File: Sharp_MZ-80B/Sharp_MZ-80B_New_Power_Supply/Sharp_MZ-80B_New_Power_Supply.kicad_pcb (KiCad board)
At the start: 2 copper layers, 139 x 125 mm, 19 parts, among them J1 +12V (NS), J2 DC In, J3 To Tape Deck, J4 To Motherboard, U1 PSU5, U2 R-78CK5.0-0.5

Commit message: Revised PSU design
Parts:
- added D2: 1.5KE15A, Diode_THT:D_DO-201AE_P15.24mm_Horizontal, F.Cu at (107.6, 56.2)
- added F1: T4A, Fuse:Littelfuse_5x20mm, F.Cu at (93.0, 67.4)
- C1: value 4700µF -> 4700µF 25V; footprint Capacitor_THT:CP_Radial_D16.0mm_P7.50mm -> Capacitor_THT:CP_Axial_L40.0mm_D16.0mm_P48.00mm_Horizontal
- C2, C4, C6, C8: footprint Capacitor_THT:C_Disc_D3.8mm_W2.6mm_P2.50mm -> Capacitor_THT:C_Disc_D4.7mm_W2.5mm_P5.00mm
- J1: value +12V (NS) -> +12V (S)
- J2: footprint Clueless_Engineer:TJC1-2A -> Connector_JST:JST_VH_B2P-VH_1x02_P3.96mm_Vertical
- R1: value 2.2Ω -> 2.2Ω 2W
- moved C1 56.8 mm to (208.6, 56.2)
- moved D1 54.3 mm to (172.4, 56.2)
- moved R1 53.6 mm to (178.1, 56.2)
- moved C4 40.4 mm to (137.5, 56.2), turned to -90 degrees
- moved C3 39.6 mm to (123.5, 56.2), turned to -90 degrees
- moved J1 29.8 mm to (147.6, 56.2)
- moved C2 29.3 mm to (193.3, 64.4)
- moved J3 24.4 mm to (147.6, 71.4)
- moved C5 17.9 mm to (117.7, 105.7)
- moved C6 17.3 mm to (115.2, 113.3)
- moved U2 16.0 mm to (112.7, 95.5)
- moved J2 10.2 mm to (93.0, 94.4), turned to 90 degrees
- moved C7 4.49 mm to (169.2, 111.4)
- moved J4 4.44 mm to (151.9, 144.4)
- moved U1 3.24 mm to (140.5, 111.4)
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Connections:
- J1 pad 1: /+12V NS -> /+12V
- J2 pad 2: /+12V -> /+12V_{IN}
- J3 pad 3: /+12V -> /+12V NS
- J4 pad 2: /-5V -> /+5V
- J4 pad 3: /+5V -> /+12V
- J4 pad 4: /+12V -> /-5V
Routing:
- net /GND: track 608.0 -> 542.3 mm
- net /+12V: track 237.5 -> 276.5 mm
- net /-5V: track 76.8 -> 115.0 mm
- net /+12V NS: track 36.8 -> 57.5 mm
- net /+5V: track 132.2 -> 112.1 mm
- net /+12V_{IN}: track 0.00 -> 11.8 mm
- net Net-(D1-K): track 6.35 -> 5.72 mm
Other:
- board text added: "+5V GND +12V (NS)"
- board text added: "GND +5V +12V (S) -5V"
- board text removed: "+5V GND +12V"
- board text removed: "Connectors: TJC1 5V Regulator: PSU5 No Noise (ezsbc.com) -5V Regulator: R-78CK5.0-0.5 (Recom)"
- board text removed: "GND -5V +5V +12V"

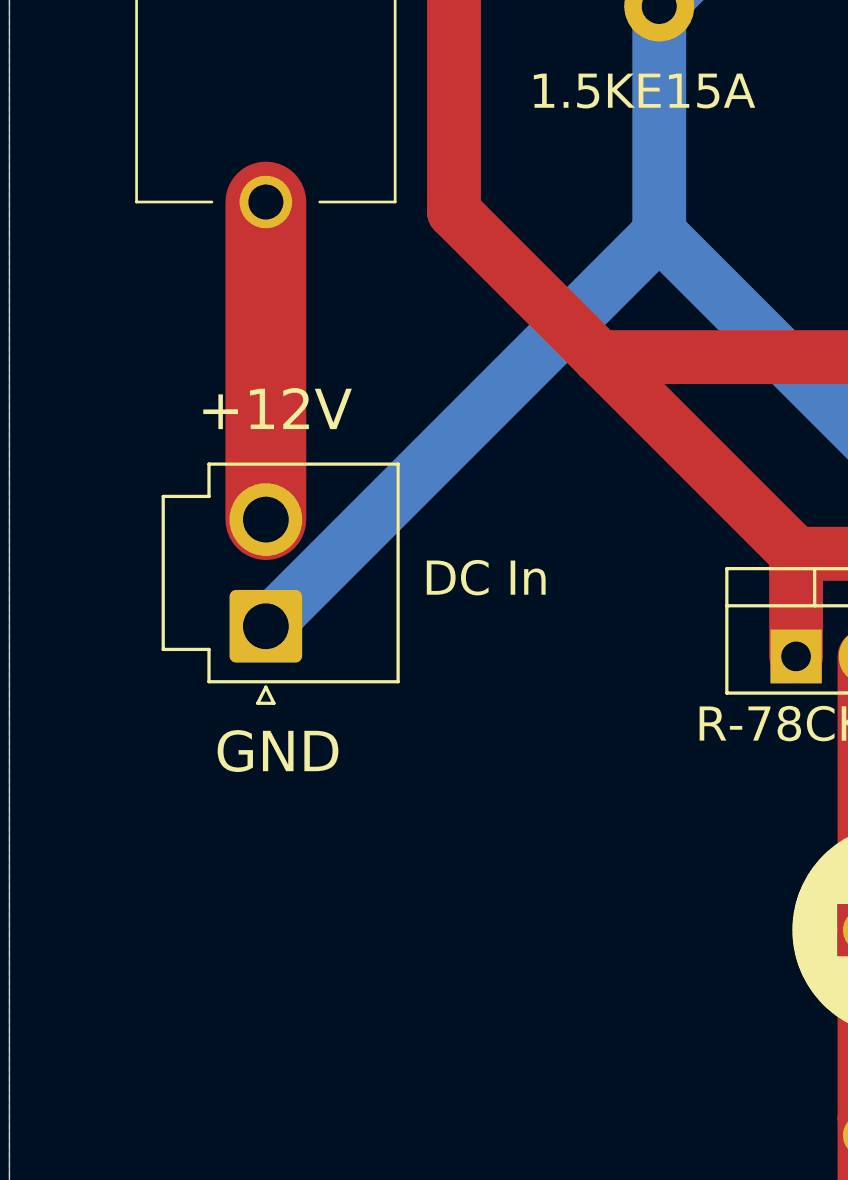
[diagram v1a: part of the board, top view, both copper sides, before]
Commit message: Revised DC input connector
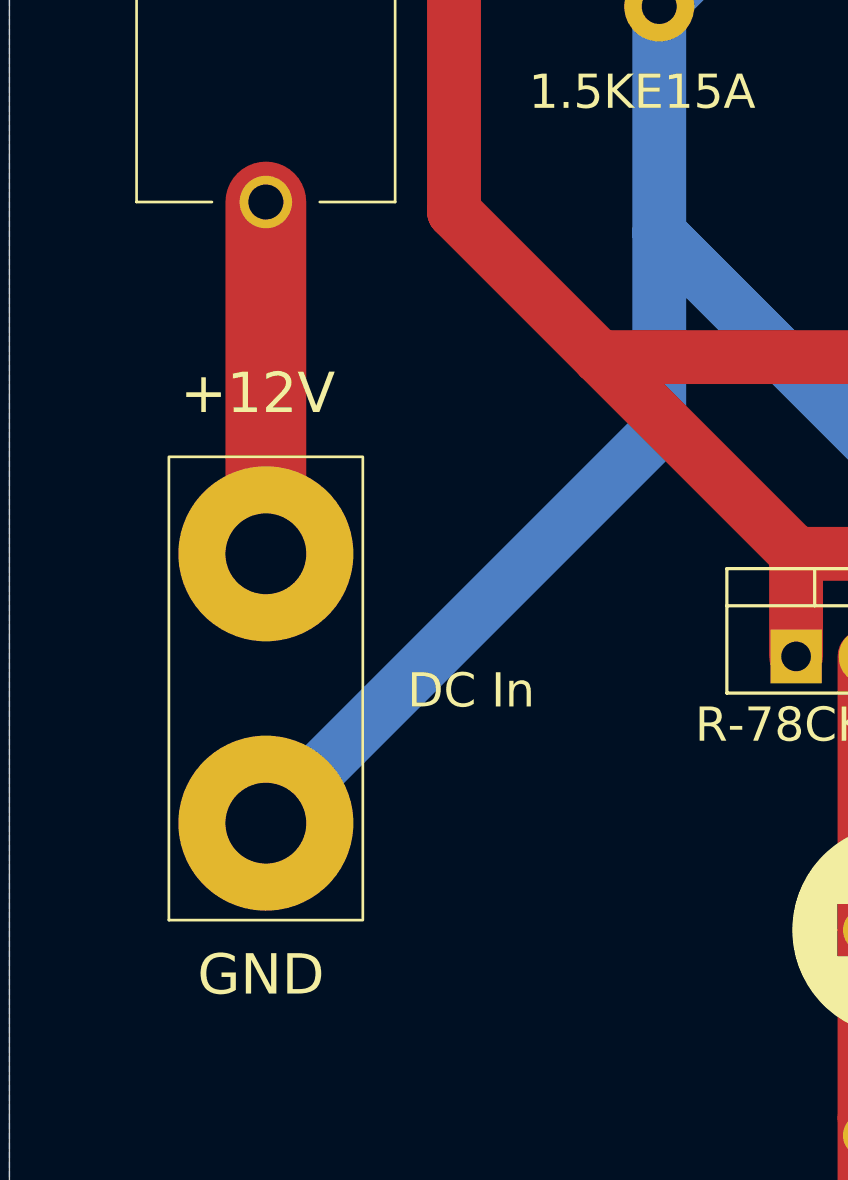
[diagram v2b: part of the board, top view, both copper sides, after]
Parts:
- J2: footprint Connector_JST:JST_VH_B2P-VH_1x02_P3.96mm_Vertical -> Clueless_Engineer:TJC1-2A
- moved J2 7.31 mm to (93.0, 101.7)
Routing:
- net /GND: track 542.3 -> 549.6 mm
- net /+12V_{IN}: track 11.8 -> 13.1 mm
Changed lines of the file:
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@@
-		)
-	)
-	(footprint "Connector_JST:JST_VH_B2P-VH_1x02_P3.96mm_Vertical"
-		(layer "F.Cu")
-		(at 93.02 94.415 90)
-		(descr "JST VH series connector, B2P-VH (http://www.jst-mfg.com/product/pdf/eng/eVH.pdf)")
-		(tags "connector JST VH vertical")
-		(property "Reference" "J2"
-			(at 1.98 -4.9 90)
-			(layer "F.SilkS")
-			(hide yes)
-			(effects
-				(font
-					(size 1 1)
-					(thickness 0.15)
-				)
-			)
-		)
-		(property "Value" "DC In"
-			(at 1.7575 8.17 0)
-			(layer "F.SilkS")
-			(effects
-				(font
-					(size 1.27 1.27)
-				)
-			)
-		)
-		(property "Datasheet" ""
-			(at 0 0 90)
-			(layer "F.Fab")
-			(hide yes)
-			(effects
-				(font
-					(size 1.27 1.27)
-				)
-			)
-		)
-		(property "Description" "Generic connector, single row, 01x02, script generated (kicad-library-utils/schlib/autogen/connector/)"
-			(at 0 0 90)
-			(layer "F.Fab")
-			(hide yes)
-			(effects
-				(font
-					(size 1.27 1.27)
-				)
-			)
-		)
-		(property "KiLib_Generator" "connector/JST"
-			(at 0 0 90)
-			(layer "F.SilkS")
-			(hide yes)
-			(effects
-				(font
-					(size 1 1)
-					(thickness 0.15)
-				)
-			)
-		)
-		(property ki_fp_filters "Connector*:*_1x??_*")
-		(sheetname "/")
-		(sheetfile "Sharp_MZ-80B_New_Power_Supply.kicad_sch")
-		(units
-			(unit
-				(name "A")
-				(pins "1" "2")
-			)
-		)
-		(attr through_hole)
-		(duplicate_pad_numbers_are_jumpers no)
-		(fp_line
-			(start 4.82 -3.81)
-			(end 4.82 -2.11)
-			(stroke
-				(width 0.12)
-				(type solid)
-			)
-			(layer "F.SilkS")
-		)
-		(fp_line
-			(start -0.86 -3.81)
-			(end 4.82 -3.81)
-			(stroke
-				(width 0.12)
-				(type solid)
-			)
-			(layer "F.SilkS")
-		)
-		(fp_line
-			(start 6.02 -2.11)
-			(end 6.02 4.91)
-			(stroke
-				(width 0.12)
-				(type solid)
-			)
-			(layer "F.SilkS")
-		)
-		(fp_line
-			(start 4.82 -2.11)
-			(end 6.02 -2.11)
-			(stroke
-				(width 0.12)
-				(type solid)
-			)
-			(layer "F.SilkS")
-		)
-		(fp_line
-			(start -0.86 -2.11)
-			(end -0.86 -3.81)
-			(stroke
-				(width 0.12)
-				(type solid)
-			)
-			(layer "F.SilkS")
-		)
-		(fp_line
-			(start -2.06 -2.11)
-			(end -0.86 -2.11)
-			(stroke
-				(width 0.12)
-				(type solid)
-			)
-			(layer "F.SilkS")
-		)
-		(fp_line
-			(start -2.86 -0.3)
-			(end -2.26 0)
-			(stroke
-				(width 0.12)
-				(type solid)
-			)
-			(layer "F.SilkS")
-		)
-		(fp_line
-			(start -2.26 0)
-			(end -2.86 0.3)
-			(stroke
-				(width 0.12)
-				(type solid)
-			)
-			(layer "F.SilkS")
-		)
-		(fp_line
-			(start -2.86 0.3)
-			(end -2.86 -0.3)
-			(stroke
-				(width 0.12)
-				(type solid)
-			)
-			(layer "F.SilkS")
-		)
-		(fp_line
-			(start 6.02 4.91)
-			(end -2.06 4.91)
-			(stroke
-				(width 0.12)
-				(type solid)
-			)
-			(layer "F.SilkS")
-		)
-		(fp_line
-			(start -2.06 4.91)
-			(end -2.06 -2.11)
-			(stroke
-				(width 0.12)
-				(type solid)
-			)
-			(layer "F.SilkS")
-		)
-		(fp_rect
-			(start -2.45 -4.2)
-			(end 6.41 5.3)
-			(stroke
-				(width 0.05)
-				(type solid)
-			)
-			(fill no)
-			(layer "F.CrtYd")
-		)
-		(fp_line
-			(start 4.71 -3.7)
-			(end 4.71 -2)
-			(stroke
-				(width 0.1)
-				(type solid)
-			)
-			(layer "F.Fab")
-		)
-		(fp_line
-			(start -0.75 -3.7)
-			(end 4.71 -3.7)
-			(stroke
-				(width 0.1)
-				(type solid)
-			)
-			(layer "F.Fab")
-		)
-		(fp_line
-			(start -0.75 -2)
-			(end -0.75 -3.7)
-			(stroke
-				(width 0.1)
-				(type solid)
-			)
-			(layer "F.Fab")
-		)
-		(fp_line
-			(start -1.95 -1)
-			(end -0.95 0)
-			(stroke
-				(width 0.1)
-				(type solid)
-			)
-			(layer "F.Fab")
-		)
-		(fp_line
-			(start -1.95 1)
-			(end -0.95 0)
-			(stroke
-				(width 0.1)
-				(type solid)
-			)
-			(layer "F.Fab")
-		)
-		(fp_rect
-			(start -1.95 -2)
-			(end 5.91 4.8)
-			(stroke
-				(width 0.1)
-				(type solid)
-			)
-			(fill no)
-			(layer "F.Fab")
-		)
-		(fp_text user "${REFERENCE}"
-			(at 1.98 4.1 90)
-			(layer "F.Fab")
-			(effects
-				(font
-					(size 1 1)
-					(thickness 0.15)
-				)
-			)
-		)
-		(pad "1" thru_hole roundrect
-			(at 0 0 90)
-			(size 2.7 2.7)
-			(drill 1.7)
-			(layers "*.Cu" "*.Mask")
-			(remove_unused_layers no)
-			(roundrect_rratio 0.092593)
-			(net "/GND")
-			(pinfunction "Pin_1_1")
-			(pintype "passive")
-		)
-		(pad "2" thru_hole circle
-			(at 3.96 0 90)
-			(size 2.7 2.7)
-			(drill 1.7)
-			(layers "*.Cu" "*.Mask")
-			(remove_unused_layers no)
-			(net "/+12V_{IN}")
-			(pinfunction "Pin_2_2")
-			(pintype "passive")
-		)
-		(embedded_fonts no)
-		(model "${KICAD10_3DMODEL_DIR}/Connector_JST.3dshapes/JST_VH_B2P-VH_1x02_P3.96mm_Vertical.step"
-			(offset
-				(xyz 0 0 0)
-			)
-			(scale
-				(xyz 1 1 1)
-			)
-			(rotate
-				(xyz 0 0 0)
-			)
 		)
 	)
@@
 			(net "/+12V")
 			(pinfunction "Pin_1_1")
+			(pintype "passive")
+		)
+		(embedded_fonts no)
+	)
+	(footprint "Clueless_Engineer:TJC1-2A"
+		(layer "F.Cu")
+		(at 93.02 101.725 90)
+		(property "Reference" "J2"
+			(at -1 -7 90)
+			(unlocked yes)
+			(layer "F.SilkS")
+			(hide yes)
+			(effects
+				(font
+					(size 1 1)
+					(thickness 0.1)
+				)
+			)
+		)
+		(property "Value" "DC In"
+			(at 4.92 7.62 0)
+			(unlocked yes)
+			(layer "F.SilkS")
+			(effects
+				(font
+					(size 1.27 1.27)
+				)
+			)
+		)
+		(property "Datasheet" ""
+			(at 0 0 90)
+			(unlocked yes)
+			(layer "F.Fab")
+			(hide yes)
+			(effects
+				(font
+					(size 1 1)
+					(thickness 0.15)
+				)
+			)
+		)
+		(property "Description" "Generic connector, single row, 01x02, script generated (kicad-library-utils/schlib/autogen/connector/)"
+			(at 0 0 90)
+			(unlocked yes)
+			(layer "F.Fab")
+			(hide yes)
+			(effects
+				(font
+					(size 1 1)
+					(thickness 0.15)
+				)
+			)
+		)
+		(property ki_fp_filters "Connector*:*_1x??_*")
+		(sheetname "/")
+		(sheetfile "Sharp_MZ-80B_New_Power_Supply.kicad_sch")
+		(units
+			(unit
+				(name "A")
+				(pins "1" "2")
+			)
+		)
+		(attr through_hole)
+		(duplicate_pad_numbers_are_jumpers no)
+		(fp_rect
+			(start -3.6 -3.6)
+			(end 13.6 3.6)
+			(stroke
+				(width 0.1)
+				(type solid)
+			)
+			(fill no)
+			(layer "F.SilkS")
+		)
+		(fp_rect
+			(start -4 -4)
+			(end 14 4)
+			(stroke
+				(width 0.05)
+				(type default)
+			)
+			(fill no)
+			(layer "F.CrtYd")
+		)
+		(fp_text user "${REFERENCE}"
+			(at -1 -4 90)
+			(unlocked yes)
+			(layer "F.Fab")
+			(effects
+				(font
+					(size 1 1)
+					(thickness 0.15)
+				)
+			)
+		)
+		(pad "1" thru_hole circle
+			(at 0 0 90)
+			(size 6.5 6.5)
+			(drill 3)
+			(layers "*.Cu" "*.Mask")
+			(remove_unused_layers no)
+			(net "/GND")
+			(pinfunction "Pin_1_1")
+			(pintype "passive")
+		)
+		(pad "2" thru_hole circle
+			(at 10 0 90)
+			(size 6.5 6.5)
+			(drill 3)
+			(layers "*.Cu" "*.Mask")
+			(remove_unused_layers no)
+			(net "/+12V_{IN}")
+			(pinfunction "Pin_2_2")
 			(pintype "passive")
 		)
@@
 	)
 	(gr_text "+12V"
-		(at 90.48 87.28 0)
+		(at 89.845 86.645 0)
 		(layer "F.SilkS")
 		(effects
@@
 	)
 	(gr_text "GND"
-		(at 91.115 99.98 0)
+		(at 90.48 108.235 0)
 		(layer "F.SilkS")
 		(effects
@@
 	)
 	(segment
-		(start 93.02 94.415)
-		(end 107.625 79.81)
-		(width 2)
-		(layer "B.Cu")
-		(net "/GND")
-	)
-	(segment
 		(start 137.47 61.165)
 		(end 144.375 61.165)
@@
 	)
 	(segment
+		(start 107.625 87.12)
+		(end 107.625 79.81)
+		(width 2)
+		(layer "B.Cu")
+		(net "/GND")
+	)
+	(segment
 		(start 90.5 153)
 		(end 143.285 153)
+		(width 2)
+		(layer "B.Cu")
+		(net "/GND")
+	)
+	(segment
+		(start 93.02 101.725)
+		(end 107.625 87.12)
 		(width 2)
 		(layer "B.Cu")
@@
 	(segment
 		(start 93.02 78.665)
-		(end 93.02 90.455)
+		(end 93.02 91.725)
 		(width 3)
 		(layer "F.Cu")
